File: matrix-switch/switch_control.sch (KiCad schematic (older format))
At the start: 119 parts, among them J33 Conn_01x02, J34 Conn_01x05, J35 Conn_01x05, J36 Conn_01x02, J37 Conn_01x02, J38 Conn_01x02, J39 Conn_01x02, J40 Conn_01x02, J41 Conn_01x02, J42 Conn_01x02, J43 Conn_01x02, U129 STP16DPPS05, U130 STP16DPPS05, U131 STP16DPPS05, U132 STP08CP05, U133 STP16DPPS05, U134 ASSR-1218, U135 ASSR-1218, U136 ASSR-1218, U137 ASSR-1218, U138 ASSR-1218, U139 ASSR-1218, U140 ASSR-1218, U141 ASSR-1218

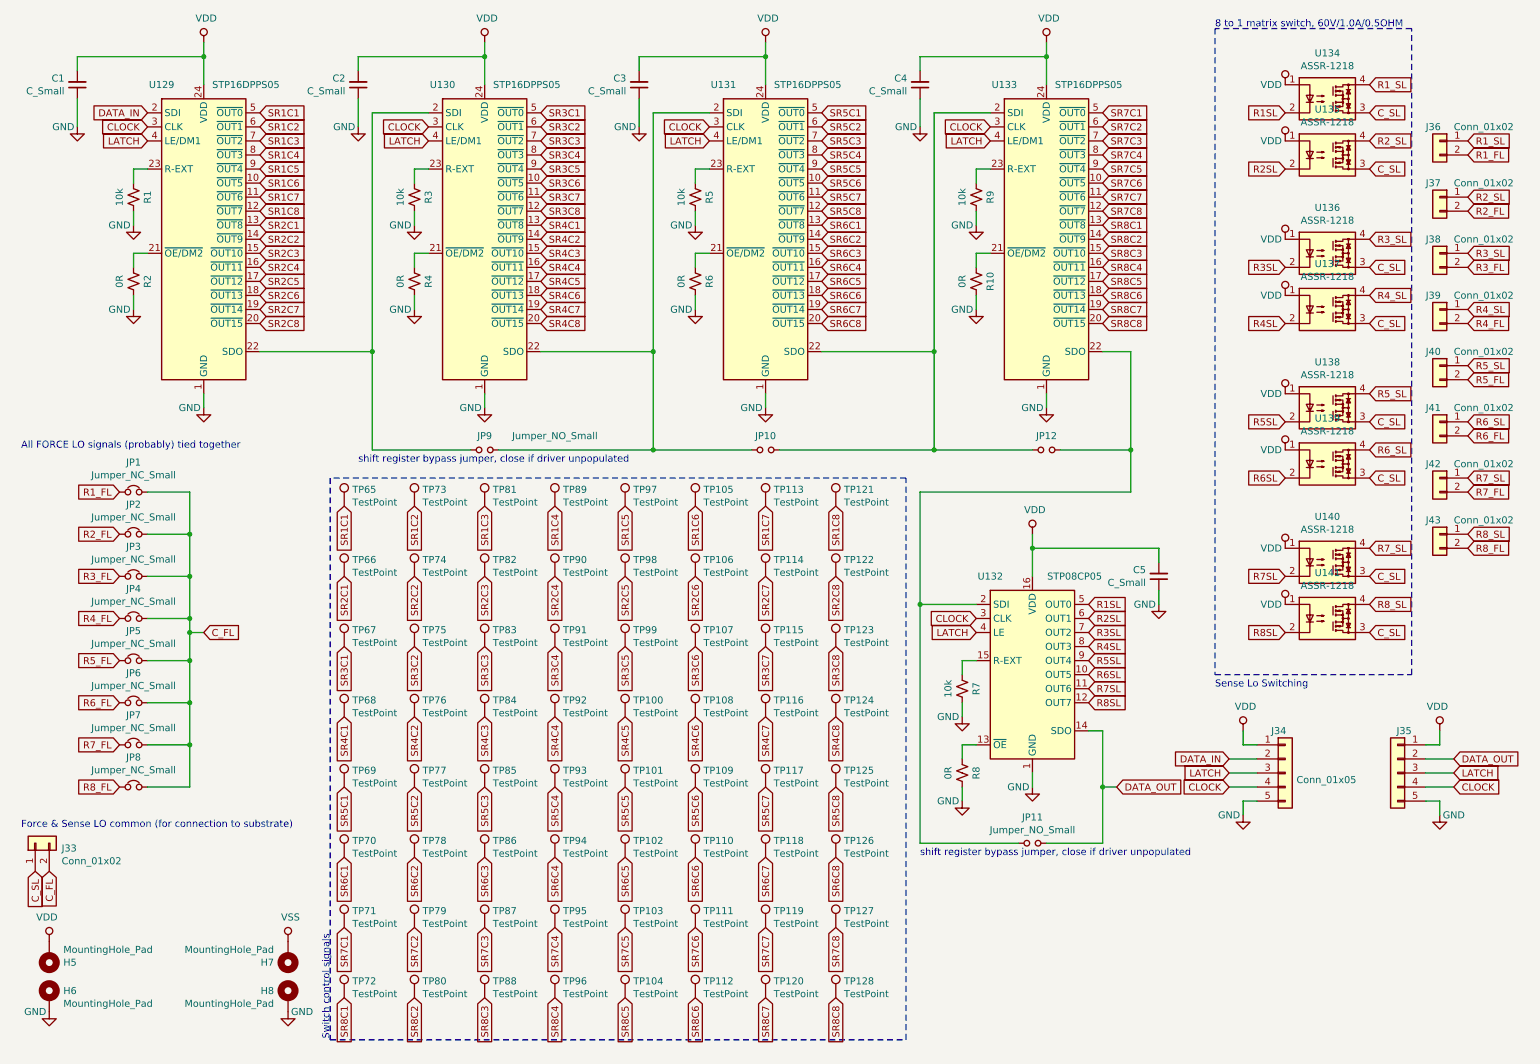
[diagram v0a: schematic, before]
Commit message: wip on matrix switch card edge adapter board
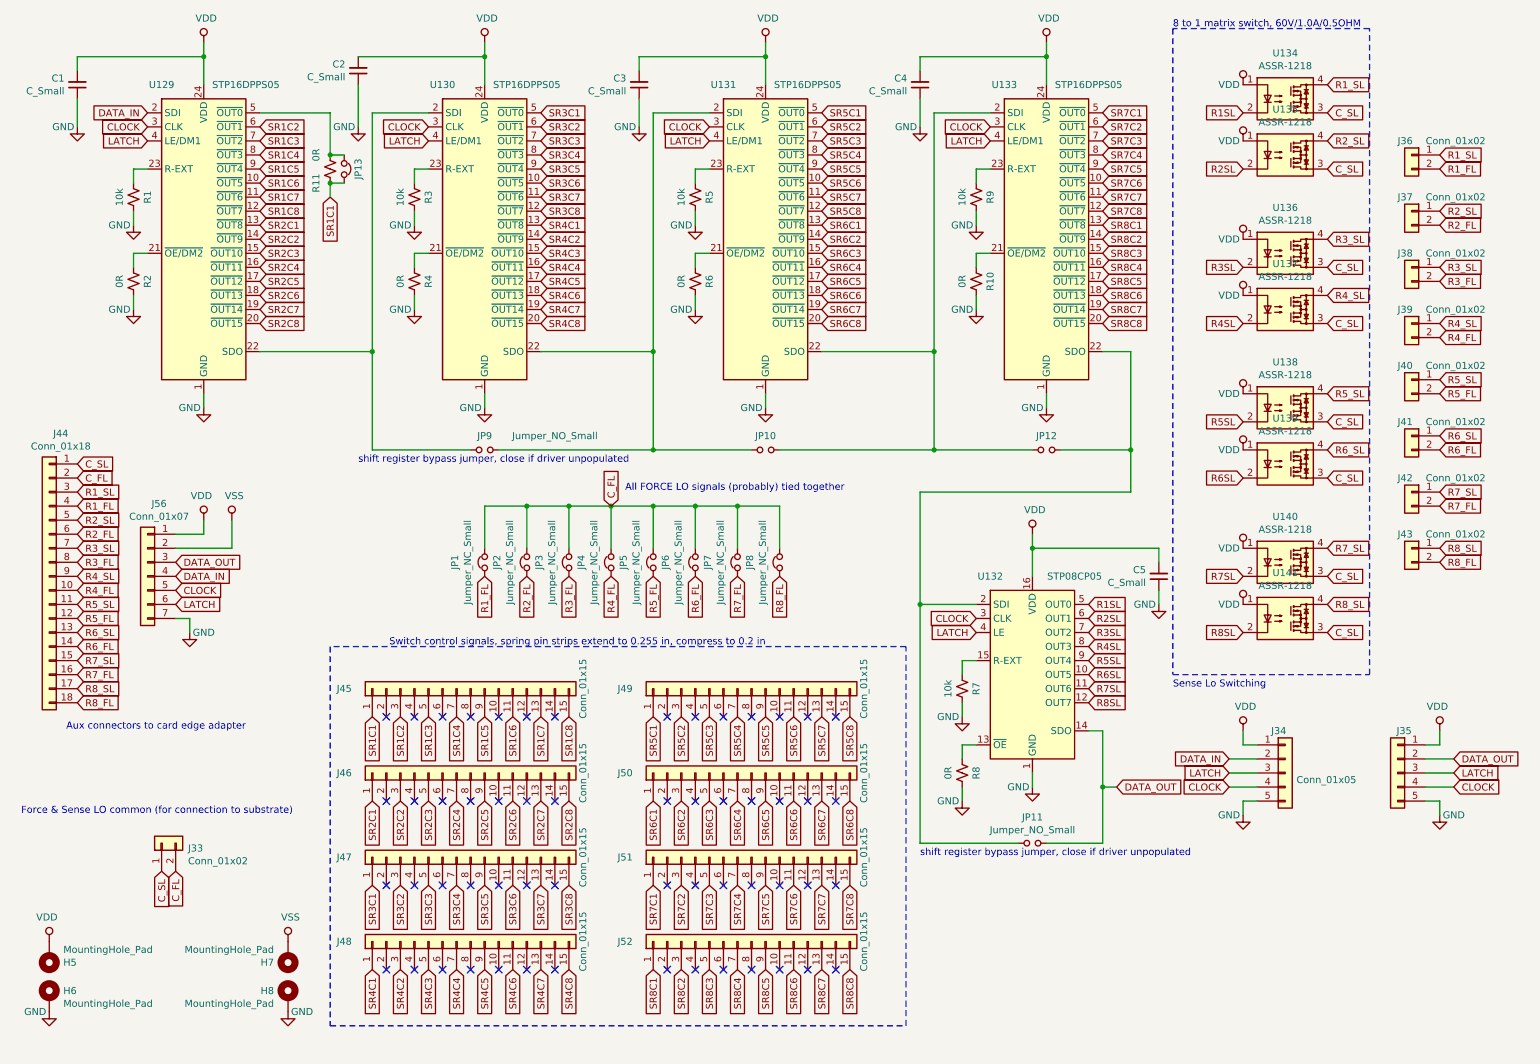
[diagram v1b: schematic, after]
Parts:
- removed TP100, TP101, TP102, TP103, TP104, TP105, TP106, TP107, TP108, TP109, TP110, TP111, TP112, TP113, TP114, TP115, TP116, TP117, TP118, TP119, TP120, TP121, TP122, TP123, TP124, TP125, TP126, TP127, TP128, TP65, TP66, TP67, TP68, TP69, TP70, TP71, TP72, TP73, TP74, TP75, TP76, TP77, TP78, TP79, TP80, TP81, TP82, TP83, TP84, TP85, TP86, TP87, TP88, TP89, TP90, TP91, TP92, TP93, TP94, TP95, TP96, TP97, TP98, TP99: TestPoint, Connector_Pin:Pin_D1.0mm_L10.0mm, symbol Connector:TestPoint
- added J44: Conn_01x18, Connector_PinHeader_2.54mm:PinHeader_1x18_P2.54mm_Vertical, symbol Connector_Generic:Conn_01x18
- added J45, J46, J47, J48, J49, J50, J51, J52: Conn_01x15, Connector_PinHeader_2.54mm:PinHeader_1x15_P2.54mm_Vertical, symbol Connector_Generic:Conn_01x15
- added J56: Conn_01x07, Connector_PinHeader_2.54mm:PinHeader_1x07_P2.54mm_Vertical, symbol Connector_Generic:Conn_01x07
- added JP13: Jumper_NC_Small, Jumper:SolderJumper-2_P1.3mm_Bridged_RoundedPad1.0x1.5mm, symbol Device:Jumper_NC_Small
- added R11: 0R, Resistor_SMD:R_0805_2012Metric, symbol Device:R_Small_US
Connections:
- net CLOCK: now also J56.5 (Pin_5)
- net C_FL: now also J44.2 (Pin_2)
- net C_SL: now also J44.1 (Pin_1)
- net DATA_IN: now also J56.4 (Pin_4)
- net DATA_OUT: now also J56.3 (Pin_3)
- net GND: now also J56.7 (Pin_7)
- net LATCH: now also J56.6 (Pin_6)
- net R1_FL: now also J44.4 (Pin_4)
- net R1_SL: now also J44.3 (Pin_3)
- net R2_FL: now also J44.6 (Pin_6)
- net R2_SL: now also J44.5 (Pin_5)
- net R3_FL: now also J44.8 (Pin_8)
- net R3_SL: now also J44.7 (Pin_7)
- net R4_FL: now also J44.10 (Pin_10)
- net R4_SL: now also J44.9 (Pin_9)
- net R5_FL: now also J44.12 (Pin_12)
- net R5_SL: now also J44.11 (Pin_11)
- net R6_FL: now also J44.14 (Pin_14)
- net R6_SL: now also J44.13 (Pin_13)
- net R7_FL: now also J44.16 (Pin_16)
- net R7_SL: now also J44.15 (Pin_15)
- net R8_FL: now also J44.18 (Pin_18)
- net R8_SL: now also J44.17 (Pin_17)
- net SR1C1: now also J45.1 (Pin_1), JP13.2, R11.2; no longer U129.5 (~OUT0)
- net SR1C2: now also J45.3 (Pin_3)
- net SR1C3: now also J45.5 (Pin_5)
- net SR1C4: now also J45.7 (Pin_7)
- net SR1C5: now also J45.9 (Pin_9)
- net SR1C6: now also J45.11 (Pin_11)
- net SR1C7: now also J45.13 (Pin_13)
- net SR1C8: now also J45.15 (Pin_15)
- net SR2C1: now also J46.1 (Pin_1)
- net SR2C2: now also J46.3 (Pin_3)
- net SR2C3: now also J46.5 (Pin_5)
- net SR2C4: now also J46.7 (Pin_7)
- net SR2C5: now also J46.9 (Pin_9)
- net SR2C6: now also J46.11 (Pin_11)
- net SR2C7: now also J46.13 (Pin_13)
- net SR2C8: now also J46.15 (Pin_15)
- net SR3C1: now also J47.1 (Pin_1)
- net SR3C2: now also J47.3 (Pin_3)
- net SR3C3: now also J47.5 (Pin_5)
- net SR3C4: now also J47.7 (Pin_7)
- net SR3C5: now also J47.9 (Pin_9)
- net SR3C6: now also J47.11 (Pin_11)
- net SR3C7: now also J47.13 (Pin_13)
- net SR3C8: now also J47.15 (Pin_15)
- net SR4C1: now also J48.1 (Pin_1)
- net SR4C2: now also J48.3 (Pin_3)
- net SR4C3: now also J48.5 (Pin_5)
- net SR4C4: now also J48.7 (Pin_7)
- net SR4C5: now also J48.9 (Pin_9)
- net SR4C6: now also J48.11 (Pin_11)
- net SR4C7: now also J48.13 (Pin_13)
- net SR4C8: now also J48.15 (Pin_15)
- net SR5C1: now also J49.1 (Pin_1)
- net SR5C2: now also J49.3 (Pin_3)
- net SR5C3: now also J49.5 (Pin_5)
- net SR5C4: now also J49.7 (Pin_7)
- net SR5C5: now also J49.9 (Pin_9)
- net SR5C6: now also J49.11 (Pin_11)
- net SR5C7: now also J49.13 (Pin_13)
- net SR5C8: now also J49.15 (Pin_15)
- net SR6C1: now also J50.1 (Pin_1)
- net SR6C2: now also J50.3 (Pin_3)
- net SR6C3: now also J50.5 (Pin_5)
- net SR6C4: now also J50.7 (Pin_7)
- net SR6C5: now also J50.9 (Pin_9)
- net SR6C6: now also J50.11 (Pin_11)
- net SR6C7: now also J50.13 (Pin_13)
- net SR6C8: now also J50.15 (Pin_15)
- net SR7C1: now also J51.1 (Pin_1)
- net SR7C2: now also J51.3 (Pin_3)
- net SR7C3: now also J51.5 (Pin_5)
- net SR7C4: now also J51.7 (Pin_7)
- net SR7C5: now also J51.9 (Pin_9)
- net SR7C6: now also J51.11 (Pin_11)
- net SR7C7: now also J51.13 (Pin_13)
- net SR7C8: now also J51.15 (Pin_15)
- net SR8C1: now also J52.1 (Pin_1)
- net SR8C2: now also J52.3 (Pin_3)
- net SR8C3: now also J52.5 (Pin_5)
- net SR8C4: now also J52.7 (Pin_7)
- net SR8C5: now also J52.9 (Pin_9)
- net SR8C6: now also J52.11 (Pin_11)
- net SR8C7: now also J52.13 (Pin_13)
- net SR8C8: now also J52.15 (Pin_15)
- net VDD: now also J56.1 (Pin_1)
- net VSS: now also J56.2 (Pin_2)
- new net: JP13.1, R11.1, U129.5 (~OUT0)
- no-connect marks 0 -> 56
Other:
- note added: "Aux connectors to card edge adapter"
- note added: "Switch control signals, spring pin strips extend to 0.255 in, compress to 0.2 in"
- note removed: "Switch control signals"
- moved on the sheet: C2, J33, J36, J37, J38, J39, J40, J41, J42, J43, JP1, JP2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
